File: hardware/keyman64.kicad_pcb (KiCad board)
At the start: 2 copper layers, 80 x 64.7 mm, 33 parts, among them J1 POWER, P1 COMPUTER, P2 KEYBOARD, P3 USB, P4 SERIAL, P5 CONTROL, SW1 RESET, SW2 BOOT, U1 MT8808, U2 ATMEGA1284P-PU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

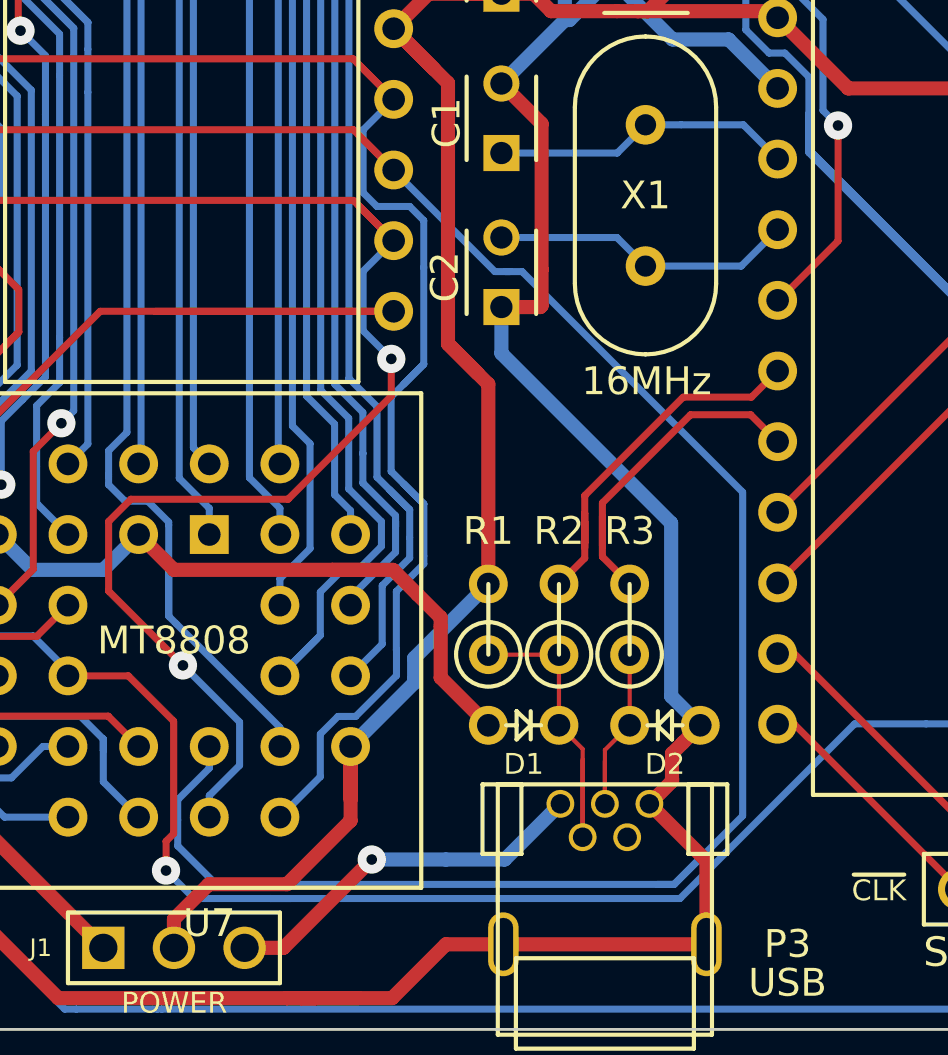
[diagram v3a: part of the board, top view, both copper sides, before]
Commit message: Hardware: Placed resistors and diodes horizontally
This allows to assemble the board as flat as possible in case there is not
much height clearance for installation.
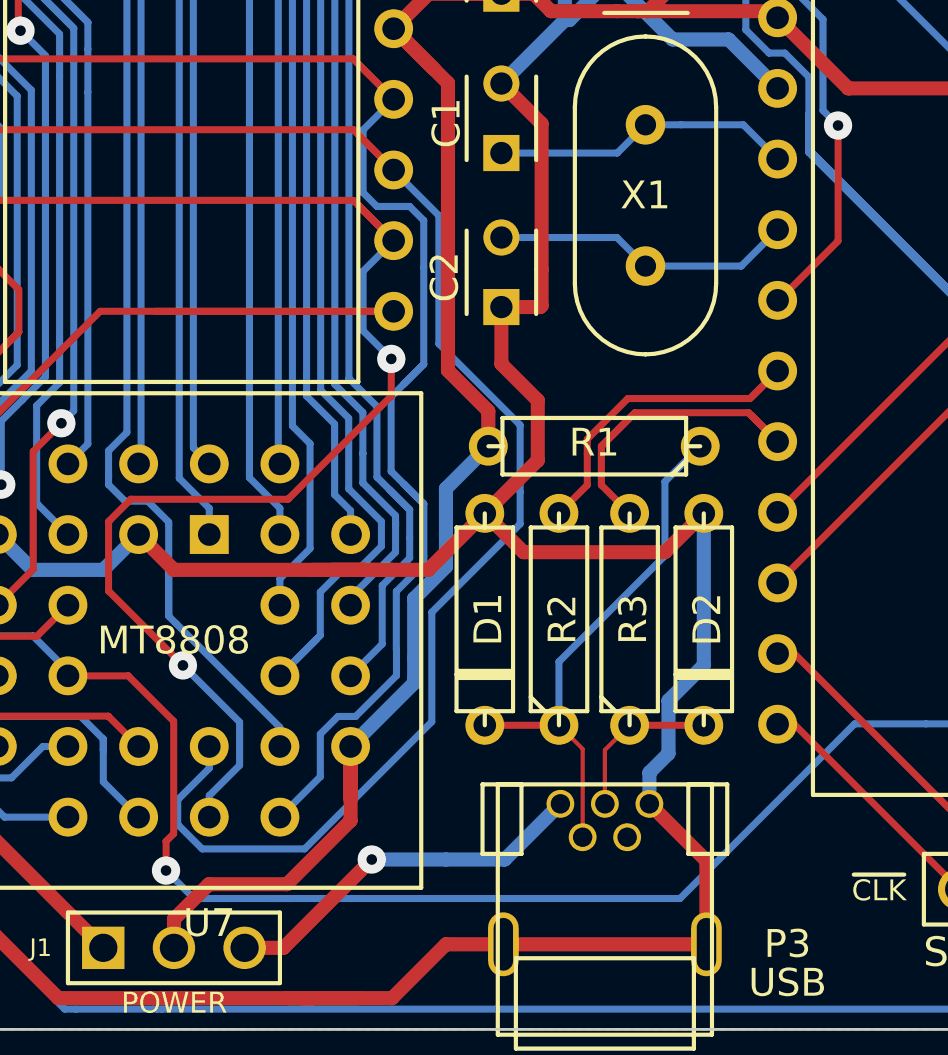
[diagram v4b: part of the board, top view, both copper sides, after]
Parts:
- D1, D2: footprint Diode:Diode-2.5mm-Vertical -> Diode:D3
- R1, R2, R3: footprint Diode:R1 -> Discret:R3
- moved R1 7.30 mm to (133.7, 110.1), turned to 180 degrees
- moved D2 4.06 mm to (137.7, 116.3), turned to 90 degrees
- moved D1 4.06 mm to (129.8, 116.3), turned to 90 degrees
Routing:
- net /B1: track 79.0 -> 59.8 mm
- net GND: track 363.8 -> 371.1 mm
- net /D-: track 12.2 -> 19.3 mm
- net Net-(R2-Pad2): track 14.3 -> 12.3 mm
- net VCC: track 186.5 -> 185.0 mm
- net /D+: track 7.29 -> 5.86 mm
- net Net-(R3-Pad2): track 12.4 -> 13.1 mm

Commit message: Hardware: Removed pin 2 on connectors for keyboard and computer
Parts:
- P1, P2: footprint pinHeaders:pinHeader-20x1 -> Diode:pinHeader-20x1
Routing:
- net GND: track 371.1 -> 372.5 mm

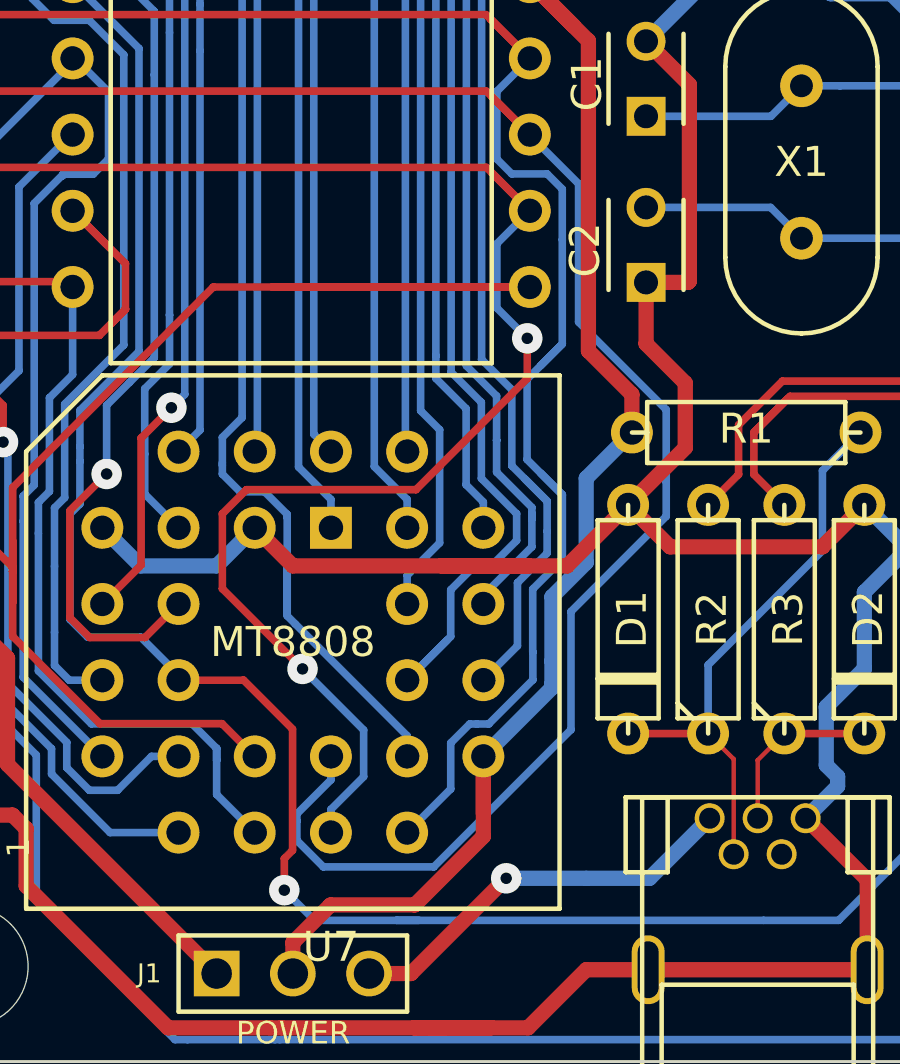
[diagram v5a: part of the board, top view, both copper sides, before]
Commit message: Hardware: Improved routing, copper fills
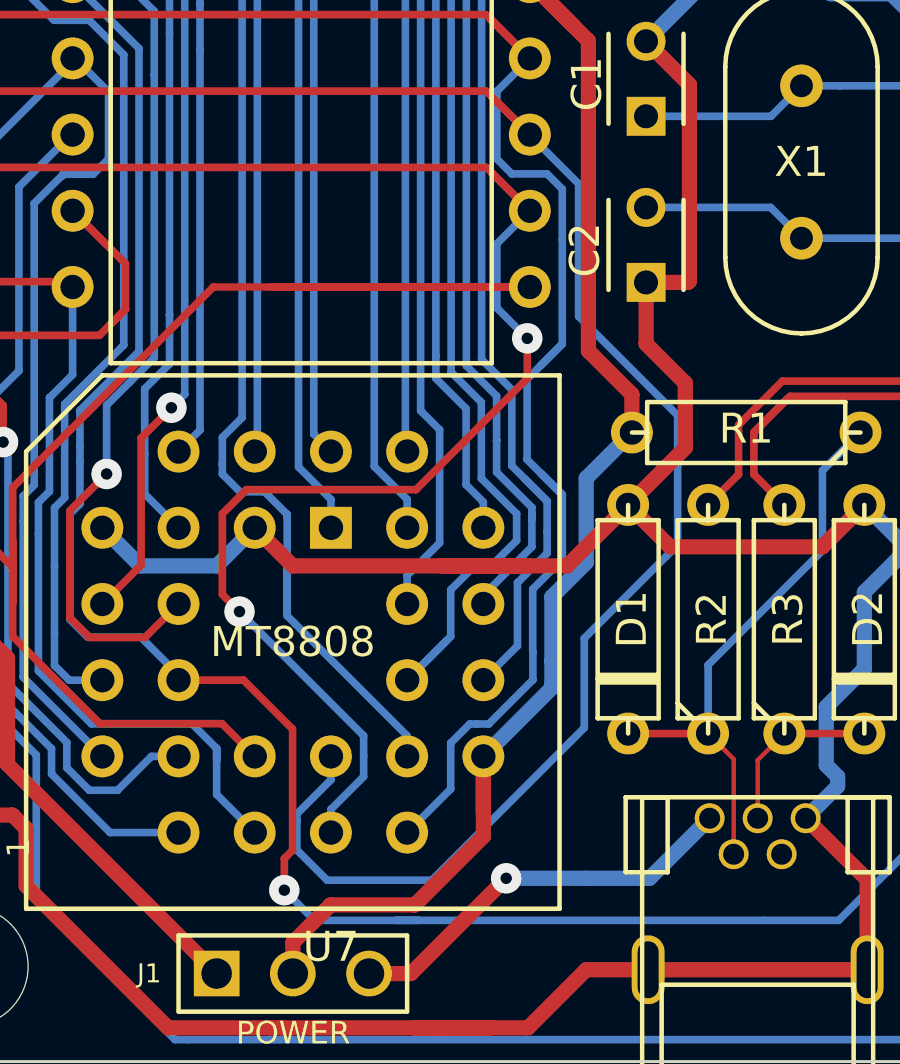
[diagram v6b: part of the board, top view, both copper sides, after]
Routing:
- net /B1: track 59.8 -> 60.9 mm
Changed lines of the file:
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@@
-(kicad_pcb (version 4) (host pcbnew 4.0.2-stable)
+(kicad_pcb (version 4) (host pcbnew 4.0.1-stable)
   (general
     (links 171)
@@
     (thickness 1.6)
     (drawings 22)
-    (tracks 1265)
+    (tracks 1271)
     (zones 0)
     (modules 33)
@@
   (segment (start 124.51374 119.8241) (end 123.88088 120.45696) (width 0.254) (layer B.Cu) (net 9))
   (segment (start 125.1958 96.3164) (end 126.517 97.6376) (width 0.254) (layer F.Cu) (net 9))
-  (segment (start 131.064 111.76) (end 131.064 112.903002) (width 0.254) (layer B.Cu) (net 10))
-  (segment (start 127.889002 120.014998) (end 123.317 124.587) (width 0.254) (layer B.Cu) (net 10))
-  (segment (start 127.889002 116.078) (end 127.889002 120.014998) (width 0.254) (layer B.Cu) (net 10))
-  (segment (start 131.064 112.903002) (end 127.889002 116.078) (width 0.254) (layer B.Cu) (net 10))
-  (segment (start 118.7534 123.063) (end 118.7534 123.7064) (width 0.254) (layer B.Cu) (net 10))
-  (segment (start 119.634 124.587) (end 123.317 124.587) (width 0.254) (layer B.Cu) (net 10))
-  (segment (start 118.7534 123.7064) (end 119.634 124.587) (width 0.254) (layer B.Cu) (net 10))
-  (segment (start 128.143 106.426) (end 128.143 101.81844) (width 0.254) (layer B.Cu) (net 10))
+  (segment (start 128.143 105.918) (end 128.143 101.81844) (width 0.254) (layer B.Cu) (net 10))
+  (segment (start 128.143 105.918) (end 128.143 106.2355) (width 0.254) (layer B.Cu) (net 10))
+  (segment (start 128.143 106.2355) (end 131.445 109.5375) (width 0.254) (layer B.Cu) (net 10))
+  (segment (start 131.445 113.8555) (end 131.064 114.2365) (width 0.254) (layer B.Cu) (net 10))
+  (segment (start 131.445 109.5375) (end 131.445 113.8555) (width 0.254) (layer B.Cu) (net 10))
+  (segment (start 128.3335 119.9515) (end 127.889002 120.395998) (width 0.254) (layer B.Cu) (net 10))
+  (segment (start 128.3335 116.967) (end 128.3335 119.9515) (width 0.254) (layer B.Cu) (net 10))
+  (segment (start 131.064 114.2365) (end 128.3335 116.967) (width 0.254) (layer B.Cu) (net 10))
+  (segment (start 118.7534 123.063) (end 118.7534 124.0239) (width 0.254) (layer B.Cu) (net 10))
+  (segment (start 123.2535 125.0315) (end 127.889002 120.395998) (width 0.254) (layer B.Cu) (net 10))
+  (segment (start 119.761 125.0315) (end 123.2535 125.0315) (width 0.254) (layer B.Cu) (net 10))
+  (segment (start 118.7534 124.0239) (end 119.761 125.0315) (width 0.254) (layer B.Cu) (net 10))
   (segment (start 128.143 101.81844) (end 126.517 100.19244) (width 0.254) (layer B.Cu) (net 10))
-  (segment (start 131.064 111.76) (end 131.064 109.347) (width 0.254) (layer B.Cu) (net 10))
-  (segment (start 131.064 109.347) (end 128.143 106.426) (width 0.254) (layer B.Cu) (net 10))
   (segment (start 126.517 100.19244) (end 126.517 100.1776) (width 0.254) (layer B.Cu) (net 10))
   (segment (start 107.378 97.4598) (end 107.3898 97.4598) (width 0.254) (layer F.Cu) (net 10))
   (segment (start 107.3898 97.4598) (end 108.66 98.73) (width 0.254) (layer F.Cu) (net 10))
+  (segment (start 108.66 98.73) (end 125.0694 98.73) (width 0.254) (layer F.Cu) (net 10))
   (segment (start 125.0694 98.73) (end 126.517 100.1776) (width 0.254) (layer F.Cu) (net 10))
-  (segment (start 108.66 98.73) (end 125.0694 98.73) (width 0.254) (layer F.Cu) (net 10))
   (segment (start 119.888 120.904) (end 119.888 121.68632) (width 0.254) (layer B.Cu) (net 10))
   (segment (start 119.888 121.68632) (end 118.7534 122.82092) (width 0.254) (layer B.Cu) (net 10))
   (segment (start 118.7534 123.063) (end 118.7534 122.82092) (width 0.254) (layer B.Cu) (net 10))
   (segment (start 125.247 98.9076) (end 126.517 100.1776) (width 0.254) (layer F.Cu) (net 10))
+  (segment (start 120.9782 120.904) (end 120.9782 120.2162) (width 0.254) (layer B.Cu) (net 11))
+  (segment (start 116.2685 114.808) (end 116.2681 114.808) (width 0.254) (layer F.Cu) (net 11))
+  (segment (start 116.2681 114.8084) (end 116.2685 114.808) (width 0.254) (layer F.Cu) (net 11))
+  (segment (start 116.2681 115.5061) (end 116.2681 114.8084) (width 0.254) (layer F.Cu) (net 11))
+  (segment (start 116.84 116.078) (end 116.2681 115.5061) (width 0.254) (layer F.Cu) (net 11))
+  (via (at 116.84 116.078) (size 1.016) (drill 0.381) (layers F.Cu B.Cu) (net 11))
+  (segment (start 120.9782 120.2162) (end 116.84 116.078) (width 0.254) (layer B.Cu) (net 11))
   (segment (start 107.378 99.9998) (end 107.3798 99.9998) (width 0.254) (layer F.Cu) (net 11))
   (segment (start 107.3798 99.9998) (end 108.65 101.27) (width 0.254) (layer F.Cu) (net 11))
@@
   (segment (start 119.888 123.444) (end 119.888 122.67184) (width 0.254) (layer B.Cu) (net 11))
   (segment (start 119.888 122.67184) (end 120.9782 121.58164) (width 0.254) (layer B.Cu) (net 11))
-  (via (at 118.9412 117.9886) (size 1.016) (layers F.Cu B.Cu) (net 11))
   (segment (start 125.247 101.4476) (end 126.517 102.7176) (width 0.254) (layer F.Cu) (net 11))
-  (segment (start 120.9782 120.0256) (end 118.9412 117.9886) (width 0.254) (layer B.Cu) (net 11))
-  (segment (start 120.9782 121.58164) (end 120.9782 120.0256) (width 0.254) (layer B.Cu) (net 11))
+  (segment (start 120.9782 121.58164) (end 120.9782 120.904) (width 0.254) (layer B.Cu) (net 11))
   (segment (start 117.0709 112.014) (end 122.7221 112.014) (width 0.254) (layer F.Cu) (net 11))
   (segment (start 116.2681 112.8168) (end 117.0709 112.014) (width 0.254) (layer F.Cu) (net 11))
-  (segment (start 116.2681 115.3155) (end 116.2681 112.8168) (width 0.254) (layer F.Cu) (net 11))
-  (segment (start 118.9412 117.9886) (end 116.2681 115.3155) (width 0.254) (layer F.Cu) (net 11))
+  (segment (start 116.2681 114.808) (end 116.2681 112.8168) (width 0.254) (layer F.Cu) (net 11))
   (segment (start 109.2787 115.7732) (end 109.2787 114.6005) (width 0.254) (layer F.Cu) (net 12))
   (segment (start 109.2787 114.6005) (end 107.378 112.6998) (width 0.254) (layer F.Cu) (net 12))

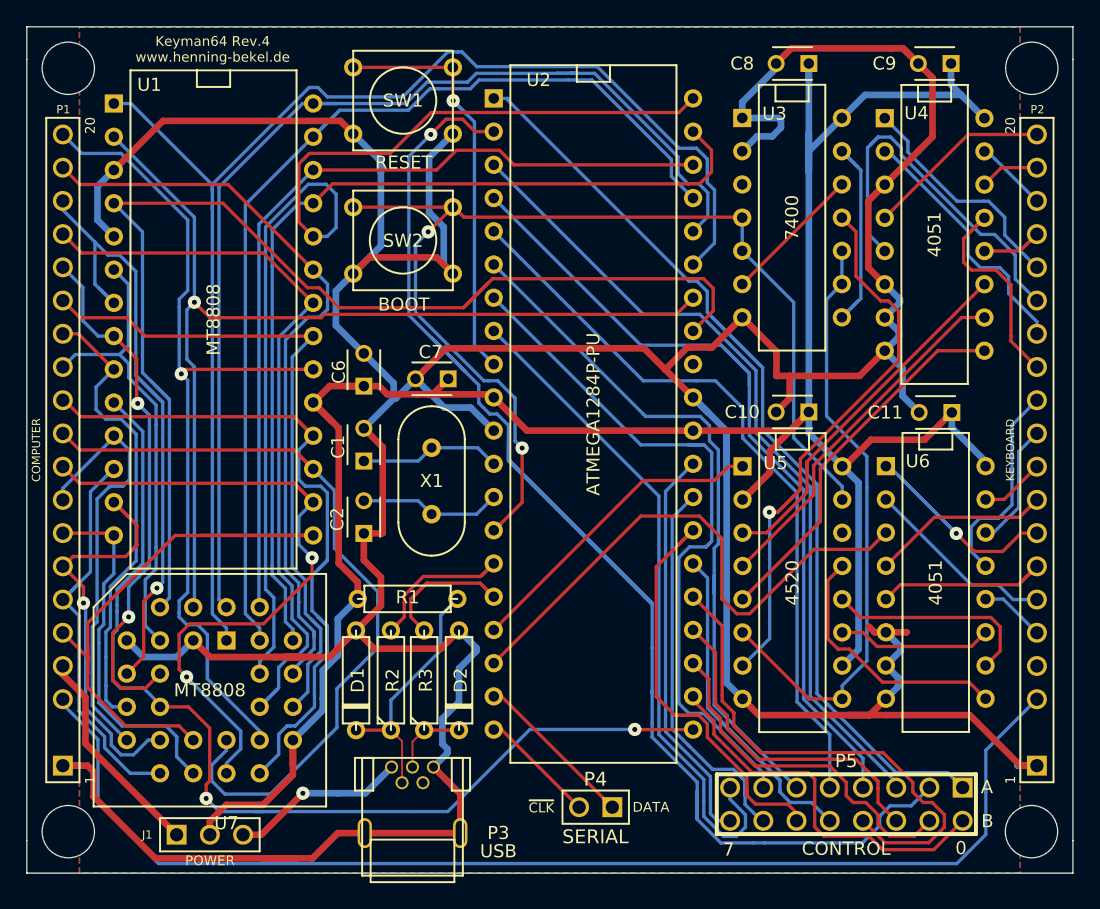
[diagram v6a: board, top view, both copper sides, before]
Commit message: Hardware: Using correct button footprints, rerouted
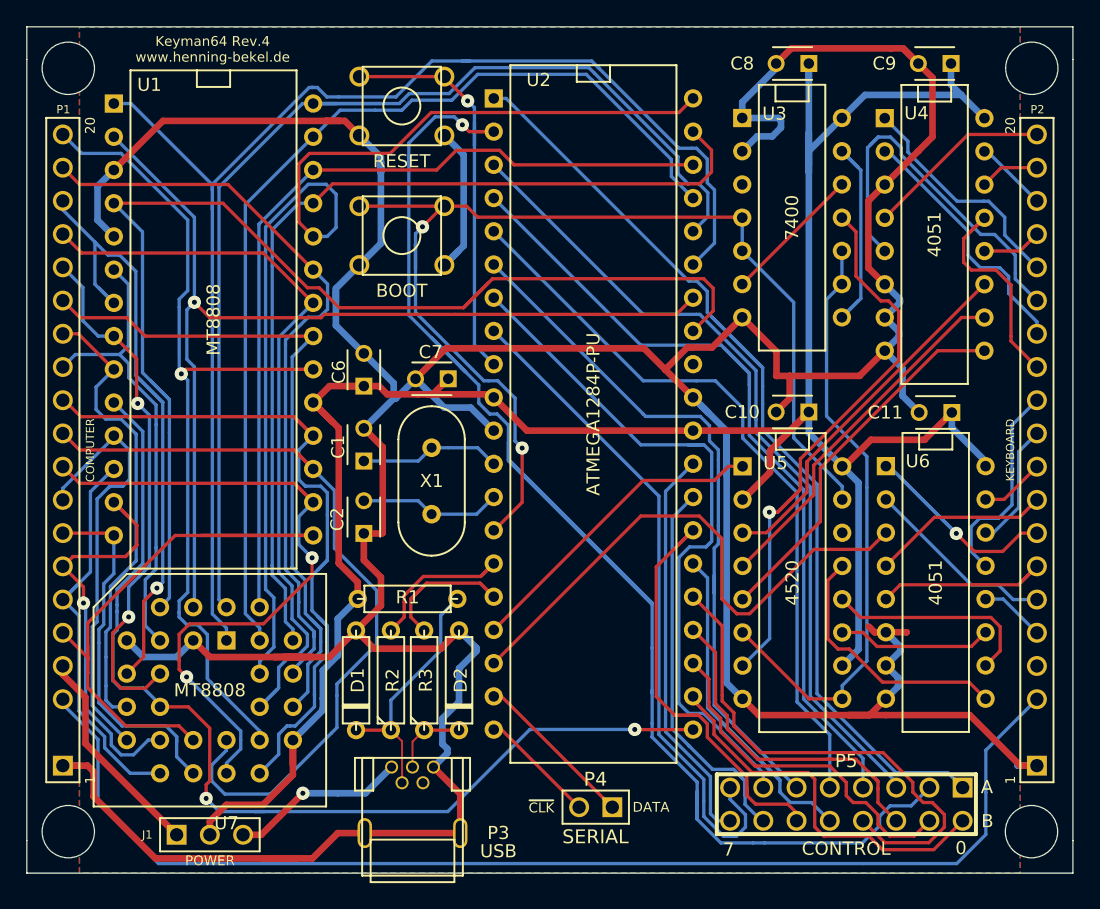
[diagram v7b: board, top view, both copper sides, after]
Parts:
- SW1, SW2: footprint Buttons_Switches_ThroughHole:SW_PUSH_SMALL -> Diode:Button
- moved SW1 4.27 mm to (130.0, 74.7)
- moved SW2 3.83 mm to (130.0, 84.6)
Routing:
- net GND: track 372.5 -> 368.1 mm
- net /CPA4: track 85.0 -> 88.7 mm
- net /UA1: track 128.0 -> 130.5 mm
- net /CPA3: track 79.1 -> 76.8 mm
- net /~RESET: track 33.1 -> 32.2 mm
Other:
- net class Default: clearance 0.0635 -> 0.25
- rule trace_clearance: 0.0635 -> 0.25
